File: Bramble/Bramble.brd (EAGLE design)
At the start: 84.8 x 55.9 mm, 17 parts

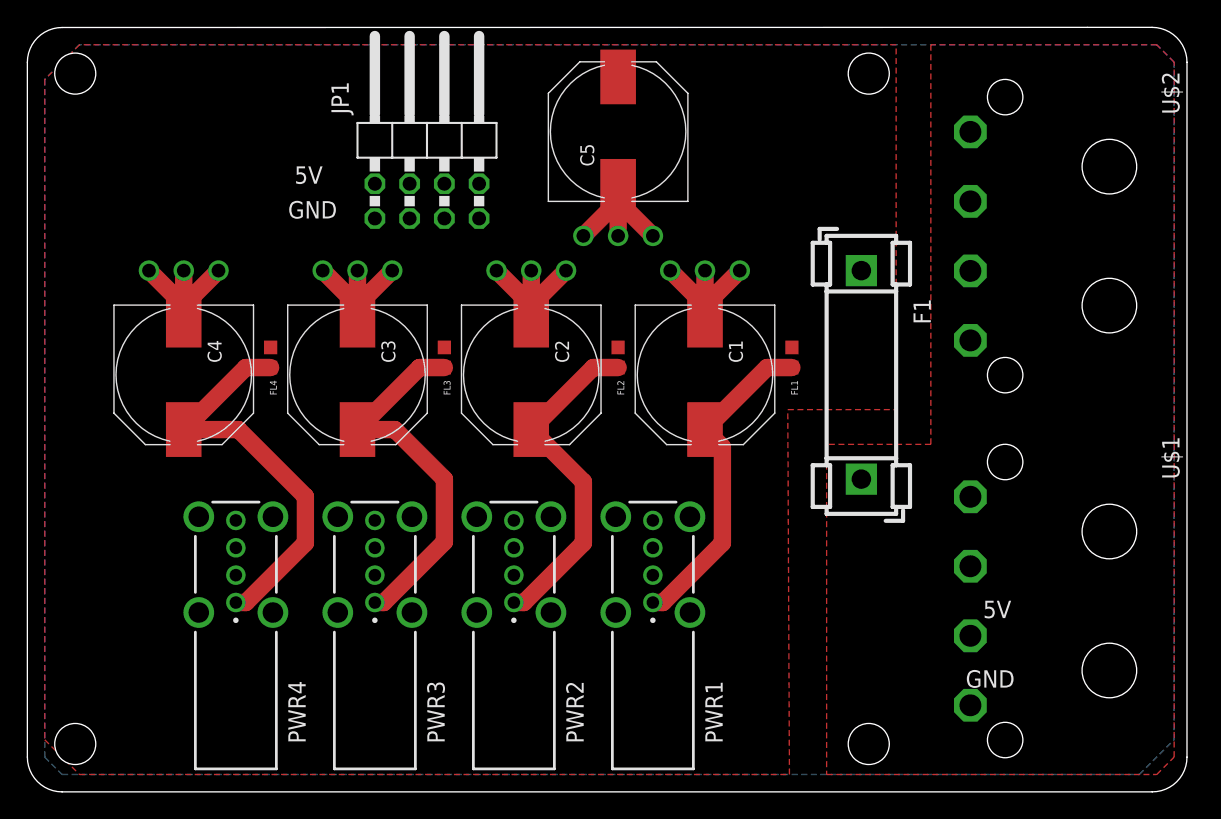
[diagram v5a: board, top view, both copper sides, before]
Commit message: Tweaked labels
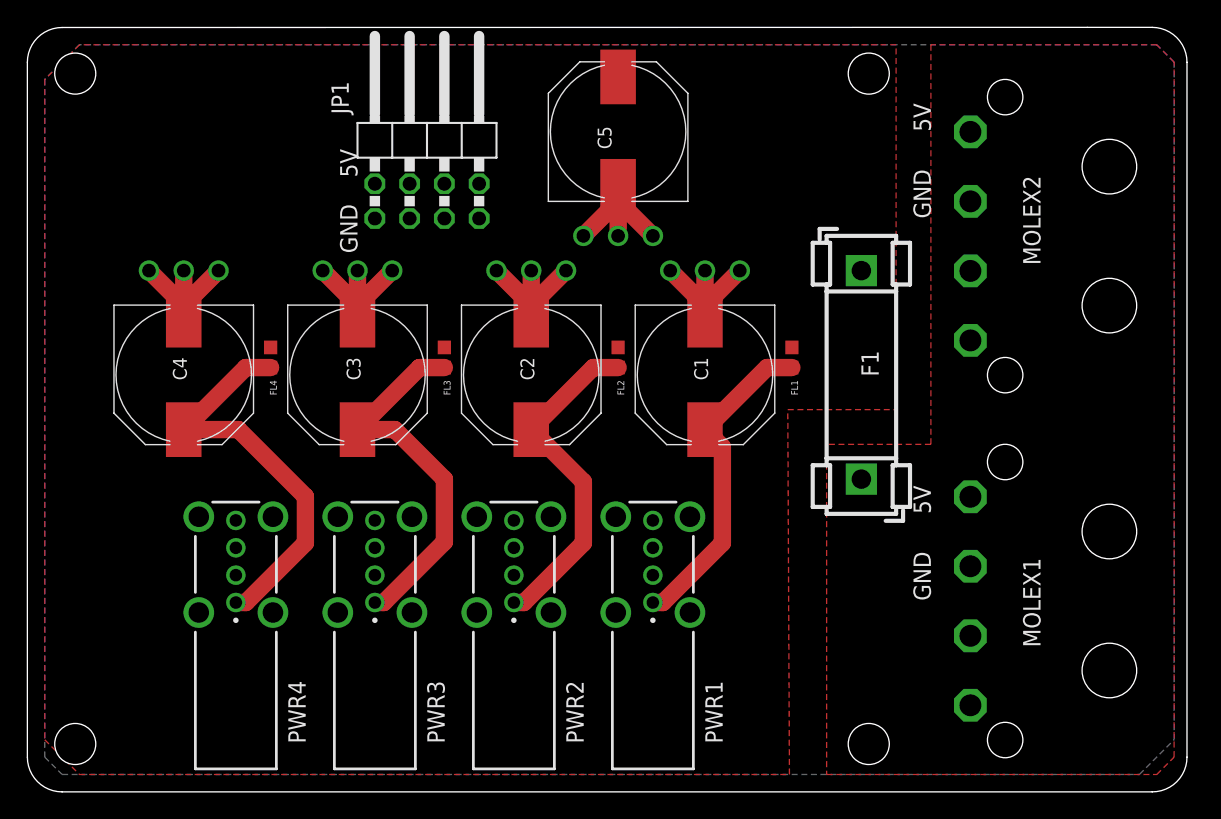
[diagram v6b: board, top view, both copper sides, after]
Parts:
- renumbered U$1 to MOLEX1, U$2 to MOLEX2
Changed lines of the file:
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@@
 <hole x="61.5" y="52.5" drill="3"/>
 <hole x="61.5" y="3.5" drill="3"/>
-<text x="69.85" y="12.7" size="1.27" layer="25">5V</text>
-<text x="68.58" y="7.62" size="1.27" layer="25">GND</text>
-<text x="19.05" y="41.91" size="1.27" layer="25">GND</text>
-<text x="21.59" y="45.72" size="1.27" layer="25" rot="R180">5V</text>
+<text x="66.04" y="20.32" size="1.27" layer="25" rot="R90">5V</text>
+<text x="66.04" y="13.97" size="1.27" layer="25" rot="R90">GND</text>
+<text x="24.13" y="39.37" size="1.27" layer="25" rot="R90">GND</text>
+<text x="22.86" y="46.99" size="1.27" layer="25" rot="R270">5V</text>
+<text x="66.04" y="48.26" size="1.27" layer="25" rot="R90">5V</text>
+<text x="66.04" y="41.91" size="1.27" layer="25" rot="R90">GND</text>
 </plain>
 <attributes>
@@
 <attribute name="MF" value="" x="60.96" y="38.1" size="1.778" layer="27" rot="R270" display="off"/>
 <attribute name="MPN" value="" x="60.96" y="38.1" size="1.778" layer="27" rot="R270" display="off"/>
-<attribute name="NAME" x="64.77" y="36.068" size="1.27" layer="25" rot="R270"/>
+<attribute name="NAME" x="60.96" y="32.258" size="1.27" layer="25" rot="R270"/>
 <attribute name="OC_FARNELL" value="unknown" x="60.96" y="38.1" size="1.778" layer="27" rot="R270" display="off"/>
 <attribute name="OC_NEWARK" value="unknown" x="60.96" y="38.1" size="1.778" layer="27" rot="R270" display="off"/>
@@
 <attribute name="THERMALLOSS" value="" x="29.21" y="48.26" size="1.778" layer="27" display="off"/>
 <attribute name="TYPE" value="" x="29.21" y="48.26" size="1.778" layer="27" display="off"/>
-<attribute name="VALUE" x="36.195" y="44.45" size="1.27" layer="27" rot="R90"/>
 </element>
 <element name="C1" library="cap-vishay-153clv" package="153CLV-1010" value="CPOL-1010" x="49.53" y="30.48" smashed="yes" rot="R270">
-<attribute name="NAME" x="51.28" y="33.03" size="1.016" layer="25" rot="R270"/>
-<attribute name="VALUE" x="46.855" y="33.03" size="1.016" layer="27" rot="R270"/>
+<attribute name="NAME" x="48.74" y="31.76" size="1.016" layer="25" rot="R270"/>
 </element>
 <element name="C2" library="cap-vishay-153clv" package="153CLV-1010" value="CPOL-1010" x="36.83" y="30.48" smashed="yes" rot="R270">
-<attribute name="NAME" x="38.58" y="33.03" size="1.016" layer="25" rot="R270"/>
-<attribute name="VALUE" x="34.155" y="33.03" size="1.016" layer="27" rot="R270"/>
+<attribute name="NAME" x="36.04" y="31.76" size="1.016" layer="25" rot="R270"/>
 </element>
 <element name="C3" library="cap-vishay-153clv" package="153CLV-1010" value="CPOL-1010" x="24.13" y="30.48" smashed="yes" rot="R270">
-<attribute name="NAME" x="25.88" y="33.03" size="1.016" layer="25" rot="R270"/>
-<attribute name="VALUE" x="21.455" y="33.03" size="1.016" layer="27" rot="R270"/>
+<attribute name="NAME" x="23.34" y="31.76" size="1.016" layer="25" rot="R270"/>
 </element>
 <element name="C4" library="cap-vishay-153clv" package="153CLV-1010" value="CPOL-1010" x="11.43" y="30.48" smashed="yes" rot="R270">
-<attribute name="NAME" x="13.18" y="33.03" size="1.016" layer="25" rot="R270"/>
-<attribute name="VALUE" x="8.755" y="33.03" size="1.016" layer="27" rot="R270"/>
+<attribute name="NAME" x="10.64" y="31.76" size="1.016" layer="25" rot="R270"/>
 </element>
 <element name="C5" library="cap-vishay-153clv" package="153CLV-1010" value="CPOL-1010" x="43.18" y="48.26" smashed="yes" rot="R90">
-<attribute name="NAME" x="41.43" y="45.71" size="1.016" layer="25" rot="R90"/>
-<attribute name="VALUE" x="45.855" y="45.71" size="1.016" layer="27" rot="R90"/>
+<attribute name="NAME" x="42.7" y="46.98" size="1.016" layer="25" rot="R90"/>
 </element>
 <element name="FL1" library="BLM18PG121SH1D" package="BEADC1608X95N" value="BLM18PG121SH1D" x="55.88" y="31.75" smashed="yes" rot="R90">
@@
 <attribute name="PRICE" value="None" x="55.88" y="31.75" size="1.778" layer="27" rot="R90" display="off"/>
 <attribute name="PURCHASE-URL" value="https://pricing.snapeda.com/search/part/BLM18PG121SH1D/?ref=eda" x="55.88" y="31.75" size="1.778" layer="27" rot="R90" display="off"/>
-<attribute name="VALUE" x="55.43" y="34.07" size="0.5" layer="27" rot="R90" align="top-left"/>
 </element>
 <element name="FL2" library="BLM18PG121SH1D" package="BEADC1608X95N" value="BLM18PG121SH1D" x="43.18" y="31.75" smashed="yes" rot="R90">
@@
 <attribute name="PRICE" value="None" x="43.18" y="31.75" size="1.778" layer="27" rot="R90" display="off"/>
 <attribute name="PURCHASE-URL" value="https://pricing.snapeda.com/search/part/BLM18PG121SH1D/?ref=eda" x="43.18" y="31.75" size="1.778" layer="27" rot="R90" display="off"/>
-<attribute name="VALUE" x="42.73" y="34.07" size="0.5" layer="27" rot="R90" align="top-left"/>
 </element>
 <element name="FL3" library="BLM18PG121SH1D" package="BEADC1608X95N" value="BLM18PG121SH1D" x="30.48" y="31.75" smashed="yes" rot="R90">
@@
 <attribute name="PRICE" value="None" x="30.48" y="31.75" size="1.778" layer="27" rot="R90" display="off"/>
 <attribute name="PURCHASE-URL" value="https://pricing.snapeda.com/search/part/BLM18PG121SH1D/?ref=eda" x="30.48" y="31.75" size="1.778" layer="27" rot="R90" display="off"/>
-<attribute name="VALUE" x="30.03" y="34.07" size="0.5" layer="27" rot="R90" align="top-left"/>
 </element>
 <element name="FL4" library="BLM18PG121SH1D" package="BEADC1608X95N" value="BLM18PG121SH1D" x="17.78" y="31.75" smashed="yes" rot="R90">
@@
 <attribute name="PRICE" value="None" x="17.78" y="31.75" size="1.778" layer="27" rot="R90" display="off"/>
 <attribute name="PURCHASE-URL" value="https://pricing.snapeda.com/search/part/BLM18PG121SH1D/?ref=eda" x="17.78" y="31.75" size="1.778" layer="27" rot="R90" display="off"/>
-<attribute name="VALUE" x="17.33" y="34.07" size="0.5" layer="27" rot="R90" align="top-left"/>
-</element>
-<element name="U$1" library="15244441" package="MOLEX_15244441" value="15244441" x="74.93" y="13.97" smashed="yes" rot="R270">
+</element>
+<element name="MOLEX1" library="15244441" package="MOLEX_15244441" value="15244441" x="74.93" y="13.97" smashed="yes" rot="R270">
 <attribute name="AVAILABILITY" value="Bad" x="74.93" y="13.97" size="1.778" layer="27" rot="R270" display="off"/>
 <attribute name="DESCRIPTION" value=" Connector Header Through Hole, Right Angle 4 position 0.200 (5.08mm) " x="74.93" y="13.97" size="1.778" layer="27" rot="R270" display="off"/>
 <attribute name="MF" value="Molex" x="74.93" y="13.97" size="1.778" layer="27" rot="R270" display="off"/>
 <attribute name="MP" value="15-24-4441" x="74.93" y="13.97" size="1.778" layer="27" rot="R270" display="off"/>
-<attribute name="NAME" x="82.9431" y="25.9896" size="1.27208125" layer="25" rot="R270"/>
+<attribute name="NAME" x="72.7831" y="17.0996" size="1.27208125" layer="25" rot="R270"/>
 <attribute name="PACKAGE" value="None" x="74.93" y="13.97" size="1.778" layer="27" rot="R270" display="off"/>
 <attribute name="PRICE" value="None" x="74.93" y="13.97" size="1.778" layer="27" rot="R270" display="off"/>
-<attribute name="VALUE" x="64.9181" y="25.9843" size="1.271509375" layer="27" rot="R270"/>
-</element>
-<element name="U$2" library="15244441" package="MOLEX_15244441" value="15244441" x="74.93" y="40.64" smashed="yes" rot="R270">
+</element>
+<element name="MOLEX2" library="15244441" package="MOLEX_15244441" value="15244441" x="74.93" y="40.64" smashed="yes" rot="R270">
 <attribute name="AVAILABILITY" value="Bad" x="74.93" y="40.64" size="1.778" layer="27" rot="R270" display="off"/>
 <attribute name="DESCRIPTION" value=" Connector Header Through Hole, Right Angle 4 position 0.200 (5.08mm) " x="74.93" y="40.64" size="1.778" layer="27" rot="R270" display="off"/>
 <attribute name="MF" value="Molex" x="74.93" y="40.64" size="1.778" layer="27" rot="R270" display="off"/>
 <attribute name="MP" value="15-24-4441" x="74.93" y="40.64" size="1.778" layer="27" rot="R270" display="off"/>
-<attribute name="NAME" x="82.9431" y="52.6596" size="1.27208125" layer="25" rot="R270"/>
+<attribute name="NAME" x="72.7831" y="45.0396" size="1.27208125" layer="25" rot="R270"/>
 <attribute name="PACKAGE" value="None" x="74.93" y="40.64" size="1.778" layer="27" rot="R270" display="off"/>
 <attribute name="PRICE" value="None" x="74.93" y="40.64" size="1.778" layer="27" rot="R270" display="off"/>
-<attribute name="VALUE" x="64.9181" y="52.6543" size="1.271509375" layer="27" rot="R270"/>
 </element>
 </elements>
@@
 <wire x1="52.07" y1="38.1" x2="49.53" y2="35.56" width="1.27" layer="1"/>
 <wire x1="49.53" y1="35.56" x2="49.53" y2="34.29" width="1.27" layer="1"/>
-<contactref element="U$1" pad="2"/>
-<contactref element="U$2" pad="2"/>
+<contactref element="MOLEX1" pad="2"/>
+<contactref element="MOLEX2" pad="2"/>
 <wire x1="49.53" y1="34.29" x2="49.53" y2="34.48" width="0" layer="19" extent="1-1"/>
 </signal>
@@
 <signal name="5VIN">
 <contactref element="F1" pad="2"/>
-<contactref element="U$1" pad="1"/>
-<contactref element="U$2" pad="1"/>
+<contactref element="MOLEX1" pad="1"/>
+<contactref element="MOLEX2" pad="1"/>
 <polygon width="1.27" layer="1">
 <vertex x="66.04" y="54.61"/>

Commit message: Tweaking
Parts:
- moved MOLEX1 1.80 mm to (76.2, 15.2)
- moved MOLEX2 1.27 mm to (76.2, 40.6)
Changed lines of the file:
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@@
 <attribute name="PURCHASE-URL" value="https://pricing.snapeda.com/search/part/BLM18PG121SH1D/?ref=eda" x="17.78" y="31.75" size="1.778" layer="27" rot="R90" display="off"/>
 </element>
-<element name="MOLEX1" library="15244441" package="MOLEX_15244441" value="15244441" x="74.93" y="13.97" smashed="yes" rot="R270">
-<attribute name="AVAILABILITY" value="Bad" x="74.93" y="13.97" size="1.778" layer="27" rot="R270" display="off"/>
-<attribute name="DESCRIPTION" value=" Connector Header Through Hole, Right Angle 4 position 0.200 (5.08mm) " x="74.93" y="13.97" size="1.778" layer="27" rot="R270" display="off"/>
-<attribute name="MF" value="Molex" x="74.93" y="13.97" size="1.778" layer="27" rot="R270" display="off"/>
-<attribute name="MP" value="15-24-4441" x="74.93" y="13.97" size="1.778" layer="27" rot="R270" display="off"/>
-<attribute name="NAME" x="72.7831" y="17.0996" size="1.27208125" layer="25" rot="R270"/>
-<attribute name="PACKAGE" value="None" x="74.93" y="13.97" size="1.778" layer="27" rot="R270" display="off"/>
-<attribute name="PRICE" value="None" x="74.93" y="13.97" size="1.778" layer="27" rot="R270" display="off"/>
+<element name="MOLEX1" library="15244441" package="MOLEX_15244441" value="15244441" x="76.2" y="15.24" smashed="yes" rot="R270">
+<attribute name="AVAILABILITY" value="Bad" x="76.2" y="15.24" size="1.778" layer="27" rot="R270" display="off"/>
+<attribute name="DESCRIPTION" value=" Connector Header Through Hole, Right Angle 4 position 0.200 (5.08mm) " x="76.2" y="15.24" size="1.778" layer="27" rot="R270" display="off"/>
+<attribute name="MF" value="Molex" x="76.2" y="15.24" size="1.778" layer="27" rot="R270" display="off"/>
+<attribute name="MP" value="15-24-4441" x="76.2" y="15.24" size="1.778" layer="27" rot="R270" display="off"/>
+<attribute name="NAME" x="74.0531" y="18.3696" size="1.27208125" layer="25" rot="R270"/>
+<attribute name="PACKAGE" value="None" x="76.2" y="15.24" size="1.778" layer="27" rot="R270" display="off"/>
+<attribute name="PRICE" value="None" x="76.2" y="15.24" size="1.778" layer="27" rot="R270" display="off"/>
 </element>
-<element name="MOLEX2" library="15244441" package="MOLEX_15244441" value="15244441" x="74.93" y="40.64" smashed="yes" rot="R270">
-<attribute name="AVAILABILITY" value="Bad" x="74.93" y="40.64" size="1.778" layer="27" rot="R270" display="off"/>
-<attribute name="DESCRIPTION" value=" Connector Header Through Hole, Right Angle 4 position 0.200 (5.08mm) " x="74.93" y="40.64" size="1.778" layer="27" rot="R270" display="off"/>
-<attribute name="MF" value="Molex" x="74.93" y="40.64" size="1.778" layer="27" rot="R270" display="off"/>
-<attribute name="MP" value="15-24-4441" x="74.93" y="40.64" size="1.778" layer="27" rot="R270" display="off"/>
-<attribute name="NAME" x="72.7831" y="45.0396" size="1.27208125" layer="25" rot="R270"/>
-<attribute name="PACKAGE" value="None" x="74.93" y="40.64" size="1.778" layer="27" rot="R270" display="off"/>
-<attribute name="PRICE" value="None" x="74.93" y="40.64" size="1.778" layer="27" rot="R270" display="off"/>
+<element name="MOLEX2" library="15244441" package="MOLEX_15244441" value="15244441" x="76.2" y="40.64" smashed="yes" rot="R270">
+<attribute name="AVAILABILITY" value="Bad" x="76.2" y="40.64" size="1.778" layer="27" rot="R270" display="off"/>
+<attribute name="DESCRIPTION" value=" Connector Header Through Hole, Right Angle 4 position 0.200 (5.08mm) " x="76.2" y="40.64" size="1.778" layer="27" rot="R270" display="off"/>
+<attribute name="MF" value="Molex" x="76.2" y="40.64" size="1.778" layer="27" rot="R270" display="off"/>
+<attribute name="MP" value="15-24-4441" x="76.2" y="40.64" size="1.778" layer="27" rot="R270" display="off"/>
+<attribute name="NAME" x="74.0531" y="45.0396" size="1.27208125" layer="25" rot="R270"/>
+<attribute name="PACKAGE" value="None" x="76.2" y="40.64" size="1.778" layer="27" rot="R270" display="off"/>
+<attribute name="PRICE" value="None" x="76.2" y="40.64" size="1.778" layer="27" rot="R270" display="off"/>
 </element>
 </elements>

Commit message: Design fix
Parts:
- moved FL1 2.54 mm to (55.9, 34.3)
- moved FL2 2.54 mm to (43.2, 34.3)
- moved FL3 2.54 mm to (30.5, 34.3)
- moved FL4 2.54 mm to (17.8, 34.3)
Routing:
- net N$3: track 29.4 -> 30.9 mm
- net N$2: track 25.0 -> 26.5 mm
- net N$4: track 27.6 -> 29.1 mm
- net N$1: track 23.9 -> 25.4 mm
